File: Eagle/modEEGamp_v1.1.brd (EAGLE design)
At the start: 100 x 80 mm, 115 parts, among them IC201 TLC277P, IC202 INA114P, IC203 INA114P, IC204 TLC277P, IC205 TLC277P, IC206 TLC277P, J201 PINHD-2X17, P201 20k, P202 20k, P203 20k, Q201 BC557, Q202 BC557, Q203 BC557, Q204 BC557, Q205 BC547, Q206 BC547, Q207 BC547, Q208 BC547

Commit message: New version!
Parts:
- removed C201: 47µF tan 1ohm, MODEEG:ES-5
- removed C202, C203: 10nF, MODEEG:C-5
- removed C204, C205: 100pF, MODEEG:C-5
- removed C208, C211, C214, C217, C225, C227: 100nF, MODEEG:C-5
- removed C209: 10pF, MODEEG:C-5
- removed C212, C216, C222, C232: 1nF, MODEEG:C-5
- removed C213: 47µF, MODEEG:EL25B
- removed C220, C229: 1µF, MODEEG:C-10
- removed C231: 220nF 5%, MODEEG:C-5
- removed C234: 33nF 5%, MODEEG:C-5
- removed IC201, IC205, IC206: TLC277P, MODEEG:DIL-08
- removed IC202, IC203: INA114P, MODEEG:DIL-08
- removed J201: PINHD-2X17, MODEEG:2X17
- removed P201, P202: 20k, MODEEG:S64Y
- removed PAD201, PAD202, R_LEG: (no value), MODEEG:WIREPAD1
- removed PAD203: U_cal, MODEEG:WIREPAD1
- removed PAD204: Cal_GND, MODEEG:WIREPAD1
- removed PAD205: COM, MODEEG:WIREPAD1
- removed PAD206: AGND, MODEEG:WIREPAD1
- removed Q201, Q203: BC557, MODEEG:TO92
- removed Q205, Q207: BC547, MODEEG:TO92
- removed R201, R202, R205, R206, R207, R208, R214, R215: 2k2, MODEEG:R-10
- removed R213: 200k, MODEEG:R-10
- removed R219, R232, R238, R239: 10k, MODEEG:R-10
- removed R220: 1k, MODEEG:R-10
- removed R221, R230: 100k, MODEEG:R-10
- removed R223, R224, R227, R231: 1M, MODEEG:R-10
- removed R228: 15k, MODEEG:R-10
- removed R229: 8.2k, MODEEG:R-10
- removed R240: 100, MODEEG:R-10
- removed SJ201, SJ202, SJ203, SJ204, SJ205, SJ206: SJ, JUMPER:SJ5X5
- removed U$10, U$11, U$12, U$13: (no value), holes:3,3
- added C1, C17: 220nf, resistor:C1206
- added C10, C9: 1nF, DISCRETE:C-5
- added C11, C2: 1µF, resistor:C1206
- added C12, C13, C14, C18, C19, C20, C21, C22, C23, C24, C25, C26, C27, C28, C3, C4, C8: 100nF, resistor:C1206
- added C15: 33nF 5%, DISCRETE:C-5
- added C16: 220nF 5%, DISCRETE:C-5
- added C5, C6: 100pF, resistor:C1206
- added C7: 10pF, resistor:C1206
- added IC1: AD780N, analog-devices:DIL08
- added IC2, IC4: INA217P, burr-brown:DIL08
- added IC3: TLC277P, BURR:DIL-08
- added P1: 20k, TRIMPOT@2:S64Y
- added Q1, Q3: BC547, NPN:TO92
- added Q2, Q4: BC557, pnp:TO92
- added R1: 25k, resistor:RTRIM64Y
- added R10, R11, R12, R4, R5, R7, R8, R9: 2k2, resistor:0207/2V
- added R13, R16: 100k, resistor:0207/2V
- added R14: 1k, resistor:0207/2V
- added R15, R18, R2: 1M, resistor:0207/2V
- added R17: 8.2k, resistor:0207/2V
- added R19, R6: 10k, resistor:0207/2V
- added R20: 15k, resistor:0207/2V
- added R21, R3: 7.5k, resistor:0207/2V
- added SJ1: (no value), jumper:SJW
- added TPB1A, TPB1B, TPB2A, TPB2B, TPB3A, TPB3B, TPIAA, TPIAB: (no value), WIREPAD:1,6/0,8
- added U$1: AD7902, EEG:QSOP20
- added U$16, U$2, U$28, U$29, U$3, U$35: AD8021, EEG:SOIC8
- added X1: RJ45-6L-B, con-tycoelectronics:RJ45-NO-SHIELD
- C206, C207, C210, C215, C218, C219, C223, C226, C230: device MODEEG:C-5 -> resistor:C1206
- C221, C228: device MODEEG:C-10 -> resistor:C1206
- C224, C233, C235, C236: device MODEEG:C-5 -> DISCRETE:C-5
- CH1+, CH1-, CH2+, CH2-: device MODEEG:WIREPAD1 -> WIREPAD:1,6/0,8
- IC204: device MODEEG:DIL-08 -> BURR:DIL-08
- P203: device MODEEG:S64Y -> TRIMPOT@2:S64Y
- Q202, Q204: device MODEEG:TO92 -> pnp:TO92
- Q206, Q208: device MODEEG:TO92 -> NPN:TO92
- R203, R204, R209, R210, R211, R212, R216, R217, R218, R222, R225, R226, R233, R234, R235, R236, R237: device MODEEG:R-10 -> resistor:0207/2V
- moved C226 44.6 mm to (25.4, 43.2), turned to 0 degrees
- moved R226 36.4 mm to (38.1, 62.2), turned to 0 degrees
- moved C223 33.8 mm to (43.2, 52.1), turned to 0 degrees
- moved C235 33.3 mm to (72.4, 59.7)
- moved R233 33.1 mm to (67.3, 59.7), turned to 90 degrees
- moved R236 31.2 mm to (62.2, 59.7), turned to 90 degrees
- moved R234 30.2 mm to (63.5, 54.6), turned to 0 degrees
- moved R222 28.9 mm to (43.2, 61.0)
- moved C219 28.4 mm to (25.4, 40.6), turned to 180 degrees
- moved IC204 28.4 mm to (34.3, 43.2), turned to 0 degrees
- moved R237 27.7 mm to (64.8, 59.7), turned to 270 degrees
- moved Q208 27.3 mm to (14.0, 50.8), turned to 270 degrees
- moved C215 25.4 mm to (38.1, 54.6), flipped to the bottom, turned to 90 degrees
- moved C221 24.0 mm to (41.9, 57.1), turned to 180 degrees
- moved Q204 22.8 mm to (19.1, 50.8), turned to 270 degrees
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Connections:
- removed net 2.0V: C202.1, IC201.3, J201.2
- removed net PWM: J201.30, R223.2
- removed net R_LEG: C212.1, C216.1, R213.1, R_LEG.1
- removed net VGND: C201.1, C204.2, C205.1, C206.2, C207.1, C208.1, C211.1, C214.2, C215.2, C217.2, C218.2, C219.2, C223.2, C225.2, C226.1, C231.1, C235.1, IC201.1, IC201.2, IC202.5, IC203.5, J201.3, P201.1, P202.2, P202.3, P203.2, P203.3, Q201.1, Q202.1, Q203.1, Q204.1, Q205.1, Q206.1, Q207.1, Q208.1, R224.1, R226.1, R229.1, R231.1, R234.1, R236.1, R238.2, R240.1
- new net N$55: C18.1, U$16.7
- new net N$56: C19.1, U$3.7
- new net N$58: C20.2, U$3.4
- new net N$59: C21.2, U$16.4
- new net N$60: C8.1, U$35.7
- new net N$61: C12.1, U$28.7
- new net N$62: C24.1, U$29.7
- new net N$63: C25.2, U$35.4
- new net N$64: C26.2, U$28.4
- new net N$65: C27.2, U$29.4
- new net N$66: R218.1, R6.1, X1.1
- new net N$67: U$1.12, X1.6
- new net N$68: U$1.19, X1.5
- new net VDD: C28.1, U$1.15, U$1.2, U$1.20, U$1.7, X1.3
- new net VREF: C13.2, C14.1, C16.1, C206.2, C207.1, C215.2, C218.2, C219.2, C22.1, C226.1, C23.2, C235.1, C3.2, C4.2, C5.1, C6.2, IC2.5, IC4.5, P1.2, P1.3, P203.2, P203.3, Q1.1, Q2.1, Q202.1, Q204.1, Q206.1, Q208.1, Q3.1, Q4.1, R15.1, R17.1, R18.1, R226.1, R234.1, R236.1, U$1.4, U$1.9, X1.2
- net +5V/2: now also C12.2, C14.2, C18.2, C19.2, C22.2, C24.2, C3.1, C8.2, IC1.2, IC2.7, IC3.8, IC4.7, U$16.8, U$2.8, U$28.8, U$29.8, U$3.8, U$35.8, X1.4; no longer C203.1, C211.2, C213.1, C217.1, C227.2, IC201.8, IC202.7, IC203.7, IC205.8, IC206.8, J201.1
- net ADIN0: now also TPB3A.1, U$1.3, U$16.2, U$16.6; no longer C233.2, C236.2, IC206.7, R235.2, SJ201.2, SJ202.2, SJ203.2
- net ADIN1: now also TPB3B.1, U$1.8, U$35.2, U$35.6; no longer C232.2, C234.2, IC205.7, R230.2, SJ204.2, SJ205.2, SJ206.2
- net AGND: now also C1.1, C13.1, C17.1, C20.1, C21.1, C23.1, C25.1, C26.1, C27.1, C28.2, C4.1, IC1.4, IC2.4, IC3.4, IC4.4, R1.3, SJ1.1, U$1.10, U$1.5, U$16.1, U$2.1, U$28.1, U$29.1, U$3.1, U$35.1, X1.8; no longer C201.2, C202.2, C203.2, C208.2, C213.2, C214.1, C225.1, C227.1, C230.1, IC201.4, IC202.4, IC203.4, IC205.4, IC206.4, J201.11, J201.13, J201.5, J201.7, J201.9, P201.3, PAD206.1
- net N$1: now also IC1.6, R1.1, U$1.1, U$1.6; no longer IC202.1, R214.1
- net N$10: now also C1.2, R3.2, U$16.3; no longer Q203.2, Q207.2, R205.2, R206.1
- net N$13: now also IC3.3, R4.2, R5.2; no longer C204.1, C209.1, Q203.3, Q207.3, R201.2, R205.1
- net N$14: now also IC2.1; no longer IC203.1
- net N$15: now also C2.2, IC4.6, TPIAB.1; no longer CH2-.1, R202.1
- net N$16: now also IC4.2, R7.2; no longer CH2+.1, R201.1
- net N$17: now also IC4.3, R10.2; no longer C220.1, IC205.3, R224.2
- net N$18: now also Q1.2, Q2.2, R7.1, R9.2; no longer C222.1, IC205.2, R220.2, R221.1
- net N$19: now also C5.2, C7.2, Q1.3, Q2.3, R8.2, R9.1; no longer P202.1, R220.1
- net N$2: now also R1.2, R2.2; no longer IC202.8, R215.1
- net N$20: now also IC2.8; no longer IC203.8
- net N$21: now also IC2.2; no longer IC203.2
- net N$22: now also Q3.2, Q4.2, R10.1, R12.2; no longer C222.2, C229.1, IC205.1, R221.2
- net N$23: now also C6.1, C7.1, Q3.3, Q4.3, R11.2, R12.1; no longer C229.2, R231.2, R232.1
- net N$24: now also CH2-.1, R8.1; no longer C232.1, IC205.6, R229.2, R230.1
- net N$25: now also IC2.6, TPIAA.1; no longer IC203.6, PAD202.1
- net N$26: now also CH2+.1, R11.1; no longer J201.4, SJ201.1
- net N$27: now also IC2.3; no longer IC203.3
- net N$28: now also U$2.3; no longer IC206.3
- net N$3: now also IC1.5, R2.1; no longer IC204.5, R214.2, R215.2
- net N$30: now also C2.1, R15.2, U$28.3; no longer PAD204.1, R238.1
- net N$31: now also C9.1, R13.1, R14.2, U$28.2; no longer J201.6, SJ202.1
- net N$33: now also P1.1, R14.1; no longer C212.2, IC201.7, R213.2
- net N$34: now also C11.1, C9.2, R13.2, TPB1B.1, U$28.6; no longer R227.1, R239.2, R240.2
- net N$35: now also IC3.1, IC3.2, R6.2; no longer J201.8, SJ203.1
- net N$36: now also C15.1, R19.2, R20.1; no longer J201.10, SJ204.1
- net N$37: now also C16.2, R20.2, U$29.3; no longer J201.12, SJ205.1
- net N$38: now also U$2.2; no longer IC206.2
- net N$4: now also U$1.14, U$1.17; no longer C220.2, IC202.6, PAD201.1
- net N$41: now also C11.2, R18.2, R19.1; no longer C216.2, IC201.6, PAD205.1, R218.1, R219.1
- net N$42: now also TPB1A.1, U$2.6; no longer IC206.1
- net N$44: now also C10.1, R16.1, R17.2, U$29.2; no longer J201.14, SJ206.1
- net N$45: now also IC4.1, R4.1; no longer IC204.6, IC204.7, R219.2
- net N$46: now also IC4.8, R5.1; no longer R223.1, R227.2
- net N$47: now also C10.2, C15.2, R16.2, R21.1, TPB2B.1, U$29.6; no longer IC201.5, P201.2
- net N$48: now also C17.2, R21.2, U$35.3; no longer PAD203.1, R239.1
- net N$49: now also U$3.2; no longer IC206.6
- net N$5: now also C233.2, C236.2, R235.2, R3.1, TPB2A.1, U$3.6; no longer IC202.2, R207.2
- net N$53: now also C230.1, U$2.7; no longer C234.1, R228.1, R232.2
- net N$54: now also C223.2, U$2.4; no longer C231.2, IC205.5, R228.2
- net N$57: now also U$3.3; no longer IC206.5
- net N$7: now also U$1.13, U$1.18, X1.7; no longer IC202.3, R206.2
- net N$8: now also U$1.11, U$1.16; no longer Q201.2, Q205.2, R207.1, R208.2
- net N$9: now also IC1.8, SJ1.2; no longer C205.2, C209.2, Q201.3, Q205.3, R202.2, R208.1
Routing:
- net N$66: track 0.00 -> 133.9 mm, vias 0 -> 1
- net ADIN1: track 133.3 -> 21.8 mm
- net VREF: track 0.00 -> 110.6 mm, vias 0 -> 7
- net AGND: track 298.8 -> 406.0 mm, vias 7 -> 13
- net ADIN0: track 114.0 -> 35.4 mm, vias 2 -> 0
- net +5V/2: track 189.5 -> 246.7 mm, vias 6 -> 10
- net N$3: track 43.2 -> 3.81 mm
- net VDD: track 0.00 -> 34.8 mm, vias 0 -> 2
- net R_LEG: track 34.0 -> 0.00 mm
- net 2.0V: track 27.3 -> 0.00 mm
- net N$5: track 4.02 -> 29.7 mm
- net N$1: track 3.81 -> 28.4 mm
- net N$47: track 6.24 -> 27.2 mm
- net N$31: track 1.91 -> 22.3 mm
- net PWM: track 19.6 -> 0.00 mm
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- added copper zone on layer 16, net VREF
- removed copper zone on layer 1, net VGND
- removed copper zone on layer 16, net VGND
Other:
- board size 100 x 80 mm -> 100 x 64.8 mm
- board text removed: "+"
- board text removed: "-"
- board text removed: "1"
- board text removed: "2"
- board text removed: "DRL"
- board text removed: "EEG"
- board text removed: "ModularEEG"
- board text removed: "The OpenEEG project 2003"
- board text removed: "amplifier v1.1.0"
- board text removed: "ch1"
- board text removed: "ch2"

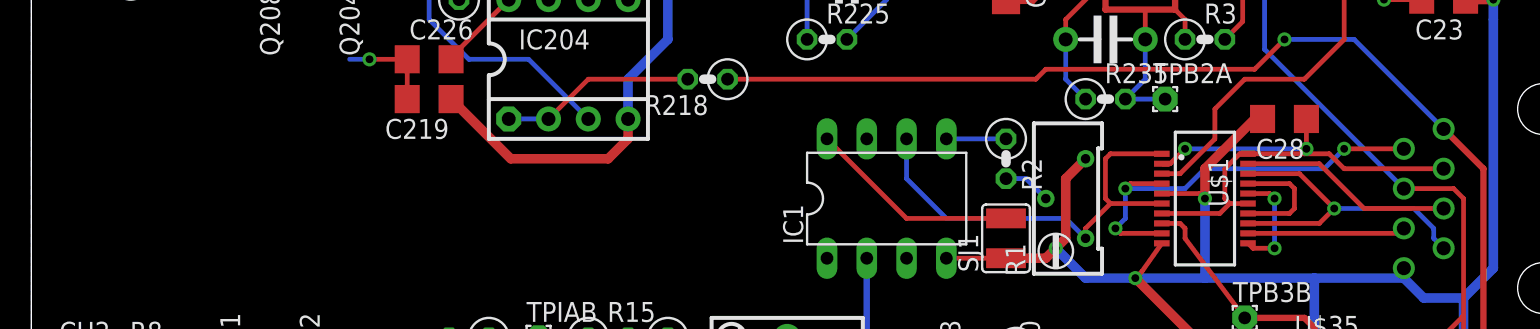
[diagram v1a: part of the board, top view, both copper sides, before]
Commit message: Added control board
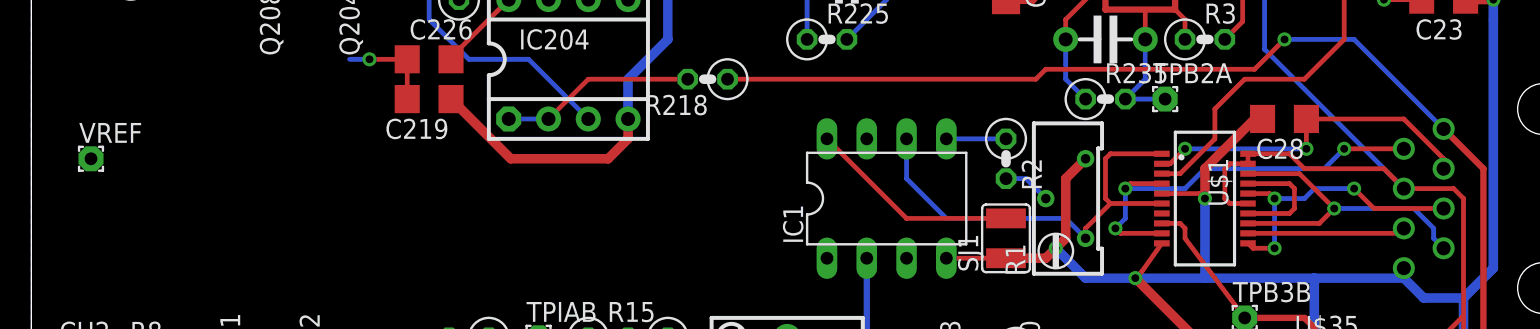
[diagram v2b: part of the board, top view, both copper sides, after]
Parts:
- added VREF: (no value), WIREPAD:1,6/0,8
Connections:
- removed net N$68: U$1.19, X1.5
- net +5V/2: now also U$1.15, U$1.19, U$1.20
- net N$8: now also X1.5
- net VDD: no longer U$1.15, U$1.20
- net VREF: now also VREF.1
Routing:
- net +5V/2: track 246.7 -> 263.4 mm
- net N$68: track 13.7 -> 0.00 mm
- net VDD: track 34.8 -> 22.0 mm
- net N$8: track 6.83 -> 18.4 mm, vias 2 -> 3
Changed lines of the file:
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@@
 <?xml version="1.0" encoding="utf-8"?>
 <!DOCTYPE eagle SYSTEM "eagle.dtd">
-<eagle version="7.2.0">
+<eagle version="7.6.0">
 <drawing>
 <settings>
@@
 </element>
 <element name="C28" library="resistor" package="C1206" value="100nF" x="80.01" y="39.37" rot="R180"/>
+<element name="VREF" library="WIREPAD" package="1,6/0,8" value=" " x="3.81" y="36.83"/>
 </elements>
 <signals>
@@
 <via x="88.9" y="12.7" extent="1-16" drill="0.5"/>
 <wire x1="88.9" y1="12.7" x2="87.63" y2="12.7" width="0.3048" layer="16"/>
+<contactref element="VREF" pad="1"/>
 </signal>
 <signal name="N$12">
@@
 <wire x1="91.44" y1="19.05" x2="91.44" y2="26.67" width="0.3048" layer="1"/>
 <wire x1="91.44" y1="26.67" x2="91.375" y2="26.735" width="0.3048" layer="1"/>
+<contactref element="U$1" pad="15"/>
+<contactref element="U$1" pad="20"/>
+<contactref element="U$1" pad="19"/>
+<wire x1="77.68" y1="37.148" x2="77.68" y2="36.513" width="0.3048" layer="1"/>
+<wire x1="77.68" y1="36.513" x2="76.518" y2="36.513" width="0.3048" layer="1"/>
+<wire x1="76.518" y1="36.513" x2="76.2" y2="36.195" width="0.3048" layer="1"/>
+<wire x1="77.68" y1="33.972" x2="76.518" y2="33.972" width="0.3048" layer="1"/>
+<wire x1="76.518" y1="33.972" x2="76.2" y2="34.29" width="0.3048" layer="1"/>
+<wire x1="76.2" y1="34.29" x2="76.2" y2="36.195" width="0.3048" layer="1"/>
+<wire x1="77.68" y1="37.148" x2="80.327" y2="37.148" width="0.3048" layer="1"/>
+<wire x1="80.327" y1="37.148" x2="81.28" y2="36.195" width="0.3048" layer="1"/>
+<wire x1="81.28" y1="36.195" x2="86.36" y2="36.195" width="0.3048" layer="1"/>
+<wire x1="86.36" y1="36.195" x2="87.63" y2="34.925" width="0.3048" layer="1"/>
 </signal>
 <signal name="N$25">
@@
 <contactref element="U$1" pad="2"/>
 <contactref element="U$1" pad="7"/>
-<contactref element="U$1" pad="15"/>
-<contactref element="U$1" pad="20"/>
 <contactref element="X1" pad="3"/>
 <contactref element="C28" pad="1"/>
-<wire x1="77.68" y1="33.972" x2="76.518" y2="33.972" width="0.3048" layer="1"/>
-<wire x1="76.518" y1="33.972" x2="76.2" y2="34.29" width="0.3048" layer="1"/>
-<wire x1="77.68" y1="37.148" x2="77.153" y2="37.148" width="0.3048" layer="1"/>
-<wire x1="77.153" y1="37.148" x2="76.2" y2="36.195" width="0.3048" layer="1"/>
-<wire x1="76.2" y1="36.195" x2="76.2" y2="34.29" width="0.3048" layer="1"/>
-<wire x1="77.68" y1="37.148" x2="81.28" y2="37.148" width="0.3048" layer="1"/>
-<wire x1="81.28" y1="37.148" x2="82.867" y2="37.148" width="0.3048" layer="1"/>
-<wire x1="82.867" y1="37.148" x2="83.82" y2="36.195" width="0.3048" layer="1"/>
-<wire x1="83.82" y1="36.195" x2="90.17" y2="36.195" width="0.3048" layer="1"/>
 <wire x1="81.41" y1="39.37" x2="81.41" y2="37.465" width="0.3048" layer="1"/>
-<wire x1="81.41" y1="37.465" x2="81.41" y2="37.278" width="0.3048" layer="1"/>
-<wire x1="81.41" y1="37.278" x2="81.28" y2="37.148" width="0.3048" layer="1"/>
-<wire x1="72.18" y1="33.337" x2="75.883" y2="33.337" width="0.3048" layer="1"/>
-<wire x1="75.883" y1="33.337" x2="76.518" y2="33.972" width="0.3048" layer="1"/>
 <wire x1="72.18" y1="36.513" x2="72.708" y2="36.513" width="0.3048" layer="1"/>
 <wire x1="72.708" y1="36.513" x2="73.66" y2="37.465" width="0.3048" layer="1"/>
@@
 <wire x1="73.66" y1="37.465" x2="81.41" y2="37.465" width="0.3048" layer="16"/>
 <via x="81.41" y="37.465" extent="1-16" drill="0.5"/>
+<wire x1="90.17" y1="36.195" x2="90.17" y2="36.83" width="0.3048" layer="1"/>
+<wire x1="90.17" y1="36.83" x2="87.63" y2="39.37" width="0.3048" layer="1"/>
+<wire x1="87.63" y1="39.37" x2="81.41" y2="39.37" width="0.3048" layer="1"/>
+<wire x1="72.18" y1="33.337" x2="72.18" y2="36.513" width="0" layer="19" extent="1-1"/>
 </signal>
 <signal name="N$1">
@@
 <wire x1="79.375" y1="31.115" x2="77.997" y2="31.115" width="0.3048" layer="1"/>
 <wire x1="77.997" y1="31.115" x2="77.68" y2="31.432" width="0.3048" layer="1"/>
+<contactref element="X1" pad="5"/>
+<wire x1="79.375" y1="34.29" x2="81.28" y2="34.29" width="0.3048" layer="16"/>
+<wire x1="81.28" y1="34.29" x2="81.915" y2="34.925" width="0.3048" layer="16"/>
+<wire x1="81.915" y1="34.925" x2="84.455" y2="34.925" width="0.3048" layer="16"/>
+<via x="84.455" y="34.925" extent="1-16" drill="0.5"/>
+<wire x1="84.455" y1="34.925" x2="85.725" y2="33.655" width="0.3048" layer="1"/>
+<wire x1="85.725" y1="33.655" x2="90.17" y2="33.655" width="0.3048" layer="1"/>
 </signal>
 <signal name="N$9">
@@
 <wire x1="87.312" y1="32.067" x2="87.63" y2="32.385" width="0.3048" layer="1"/>
 </signal>
-<signal name="N$68">
-<contactref element="U$1" pad="19"/>
-<contactref element="X1" pad="5"/>
-<wire x1="77.68" y1="36.513" x2="82.232" y2="36.513" width="0.3048" layer="1"/>
-<wire x1="82.232" y1="36.513" x2="85.09" y2="33.655" width="0.3048" layer="1"/>
-<wire x1="85.09" y1="33.655" x2="90.17" y2="33.655" width="0.3048" layer="1"/>
-</signal>
 <signal name="N$66">

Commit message: Finished digital board
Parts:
- removed IC1: AD780N, analog-devices:DIL08
- removed SJ1: (no value), jumper:SJW
- added C29, C30: 100nF, resistor:C1206
- added IC5: TLC277P, BURR:DIL-08
- R1: value 25k -> 10k; device resistor:RTRIM64Y -> resistor:0207/2V
- R2: value 1M -> 10k
- moved C28 15.3 mm to (68.6, 29.2), turned to 270 degrees
- moved R1 12.7 mm to (54.6, 34.3), turned to 270 degrees
- moved R2 9.92 mm to (54.6, 30.5), turned to 90 degrees
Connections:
- net VREF renamed VCOM
- removed net VDD: C28.1, U$1.2, U$1.7, X1.3
- new net N$68: C30.1, IC5.8
- net +5V/2: now also C30.2, R2.1; no longer IC1.2
- net AGND: now also C29.1, R1.1; no longer IC1.4, R1.3, SJ1.1
- net N$1: now also X1.3; no longer IC1.6, R1.1
- net N$2: now also C28.1, IC5.1, IC5.2, U$1.2, U$1.7; no longer R1.2, R2.2
- net N$3: now also C29.2, IC5.4; no longer IC1.5, R2.1
- net N$9: now also IC5.3, R1.2, R2.2; no longer IC1.8, SJ1.2
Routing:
- net VDD: track 22.0 -> 0.00 mm, vias 2 -> 0
- net N$2: track 3.07 -> 19.0 mm, vias 0 -> 2
- net AGND: track 406.0 -> 414.2 mm, vias 13 -> 14
- net N$1: track 28.4 -> 32.7 mm, vias 0 -> 2
- net N$68: track 0.00 -> 2.59 mm
- net +5V/2: track 263.4 -> 264.6 mm
- net VCOM: track 110.6 -> 109.5 mm
- net ADIN1: track 21.8 -> 22.9 mm

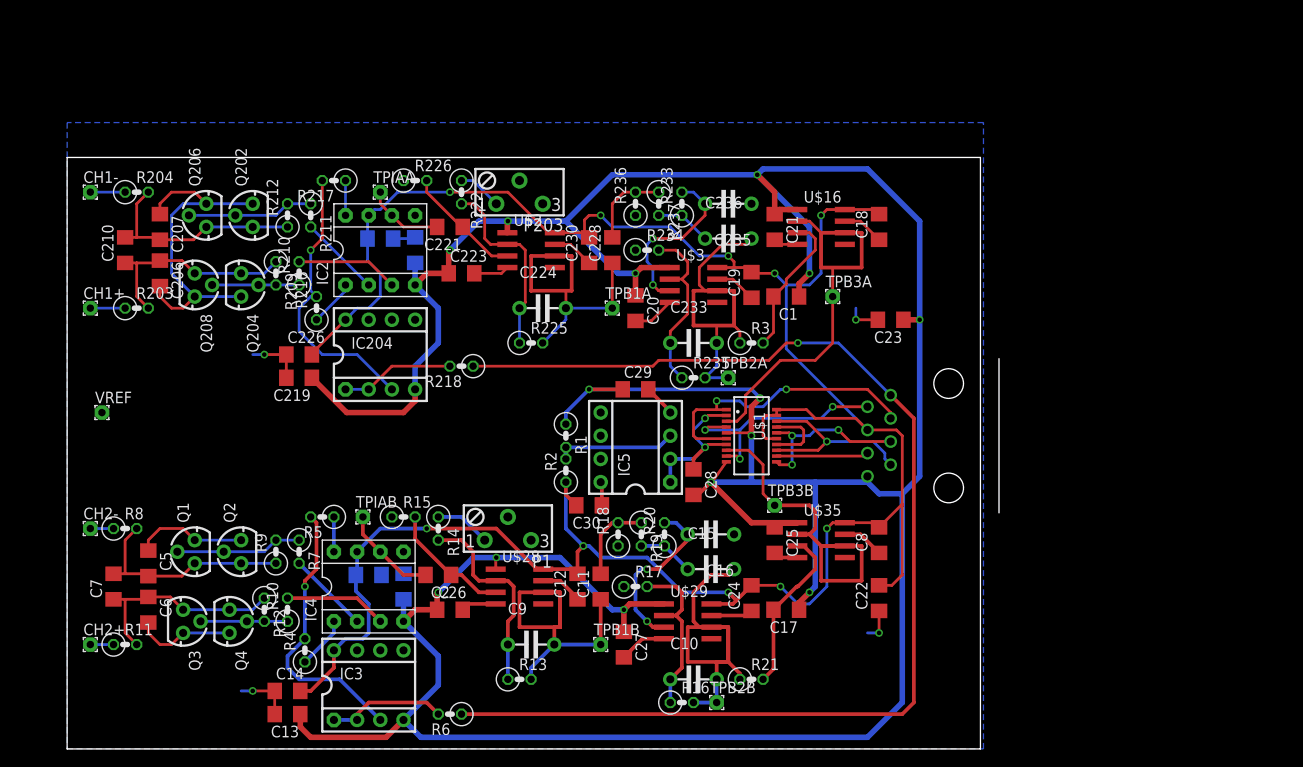
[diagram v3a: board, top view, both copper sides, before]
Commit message: Switched to DB25
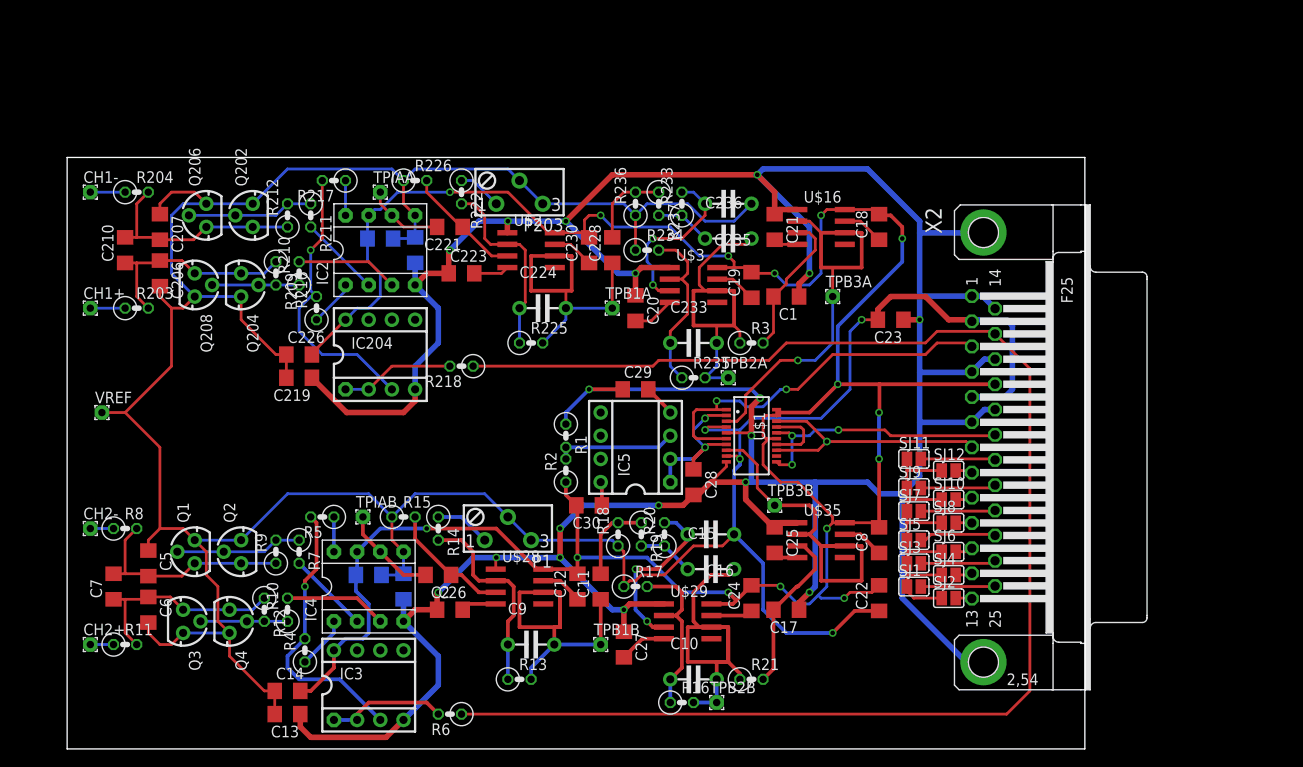
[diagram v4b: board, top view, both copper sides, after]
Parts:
- removed X1: RJ45-6L-B, con-tycoelectronics:RJ45-NO-SHIELD
- added SJ1, SJ10, SJ11, SJ12, SJ2, SJ3, SJ4, SJ5, SJ6, SJ7, SJ8, SJ9: (no value), jumper:SJ
- added X2: (no value), con-subd:F25HP
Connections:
- removed net N$67: U$1.12, X1.6
- new net N$69: SJ1.2, X2.25
- new net N$70: SJ2.2, X2.13
- new net N$71: SJ3.2, X2.24
- new net N$72: SJ4.2, X2.12
- new net N$73: SJ5.2, X2.23
- new net N$74: SJ6.2, X2.11
- new net N$75: SJ7.2, X2.22
- new net N$76: SJ8.2, X2.10
- new net N$77: SJ12.2, X2.8
- new net N$78: SJ11.2, X2.20
- new net N$79: SJ9.2, X2.21
- new net N$80: SJ10.2, X2.9
- new net N$81: SJ1.1, SJ10.1, SJ11.1, SJ12.1, SJ2.1, SJ3.1, SJ4.1, SJ5.1, SJ6.1, SJ7.1, SJ8.1, SJ9.1
- net +5V/2: now also X2.17; no longer X1.4
- net AGND: now also X2.1, X2.14, X2.16, X2.18, X2.4, X2.6; no longer X1.8
- net N$1: now also X2.3; no longer X1.3
- net N$66: now also X2.15; no longer X1.1
- net N$7: now also X2.7; no longer X1.7
- net N$8: now also X2.19; no longer X1.5
- net VCOM: now also X2.2, X2.5; no longer X1.2
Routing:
- net VCOM: track 109.5 -> 374.5 mm, vias 7 -> 4
- net N$81: track 0.00 -> 37.7 mm
- net N$66: track 133.9 -> 162.8 mm, vias 1 -> 0
- net +5V/2: track 264.6 -> 290.3 mm, vias 10 -> 15
- net N$8: track 18.4 -> 29.6 mm
- net AGND: track 414.2 -> 403.4 mm, vias 14 -> 18
- net N$67: track 10.1 -> 0.00 mm
- net N$1: track 32.7 -> 42.2 mm
- net N$73: track 0.00 -> 8.44 mm
- net N$79: track 0.00 -> 8.25 mm
- net N$71: track 0.00 -> 8.24 mm
- net N$78: track 0.00 -> 8.17 mm
- net N$75: track 0.00 -> 8.16 mm
- net N$69: track 0.00 -> 8.15 mm
- net N$7: track 20.7 -> 28.5 mm
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- removed copper zone on layer 16, net VCOM
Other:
- board size 100 x 64.8 mm -> 111.4 x 64.8 mm
